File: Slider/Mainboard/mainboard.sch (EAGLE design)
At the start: 11 parts, among them IC1 7805TV, U1 ATMEGA328P_PDIP

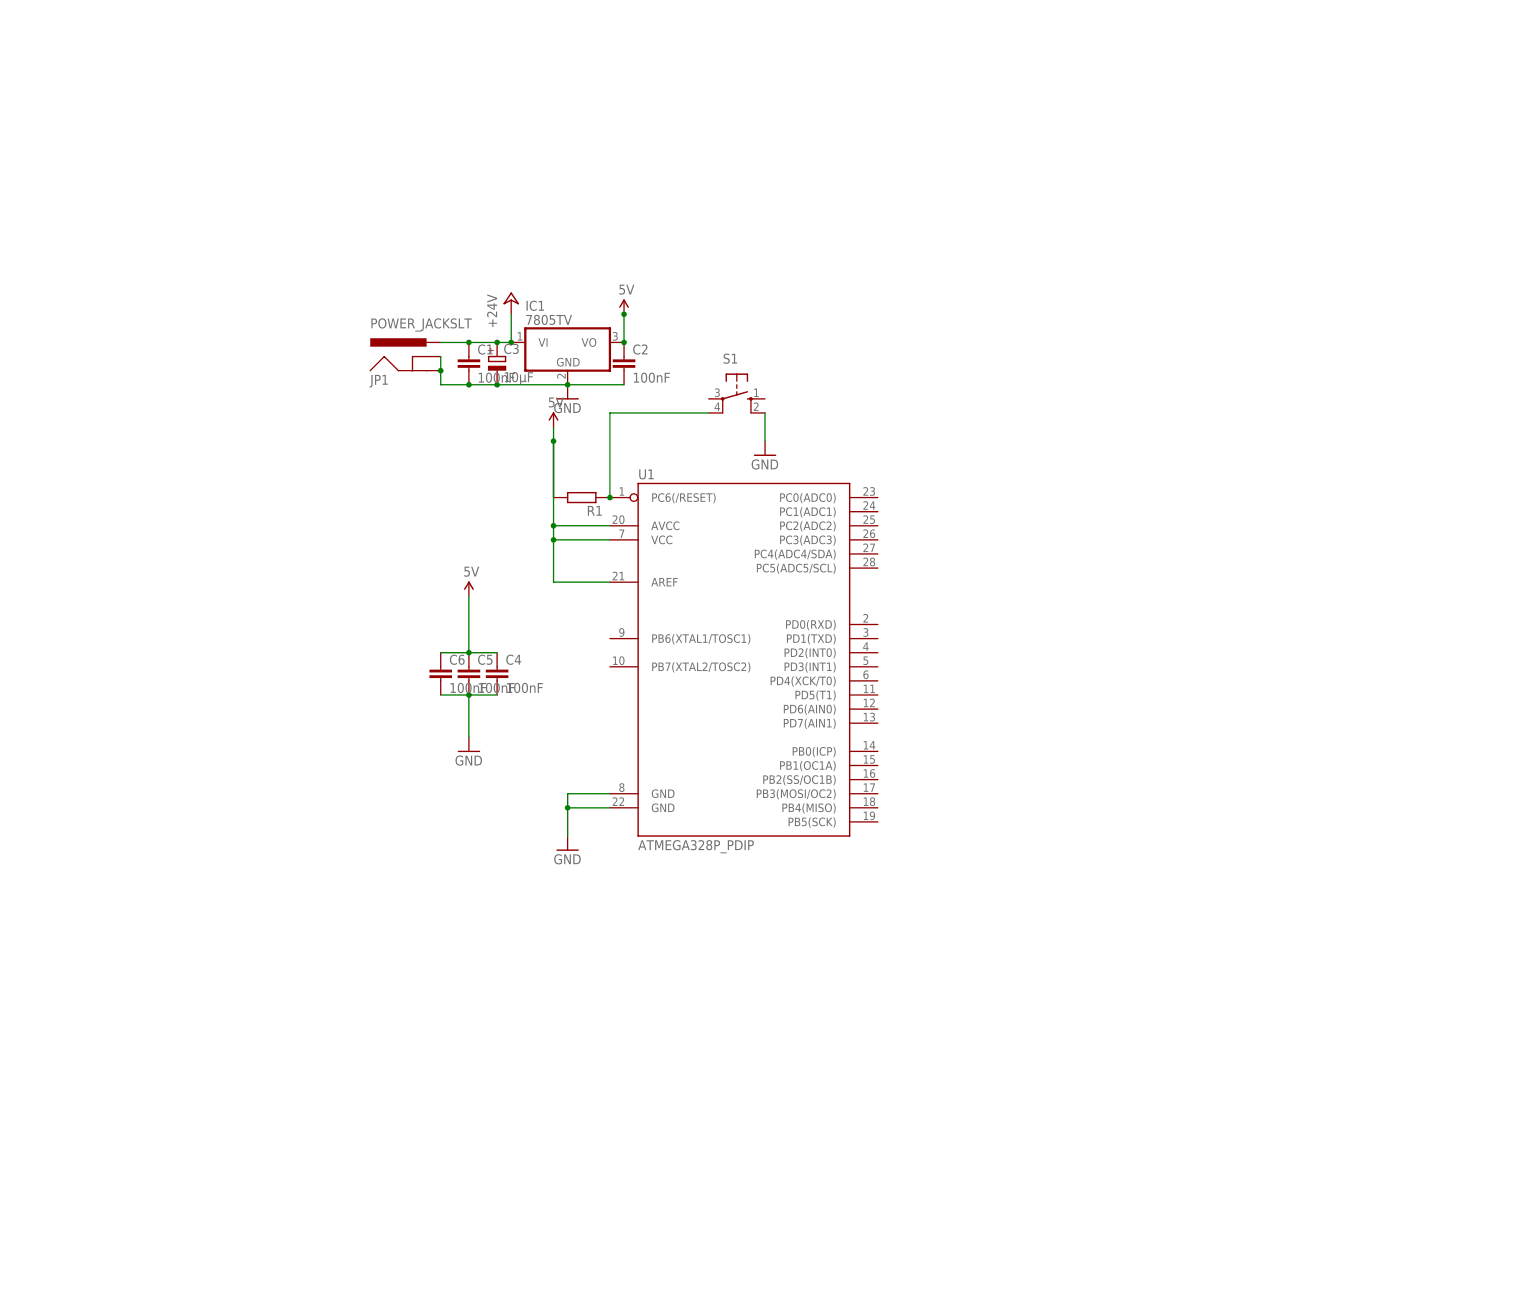
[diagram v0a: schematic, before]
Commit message: Added Motor Drivers, Serial Interface and ICSP Header to schematic
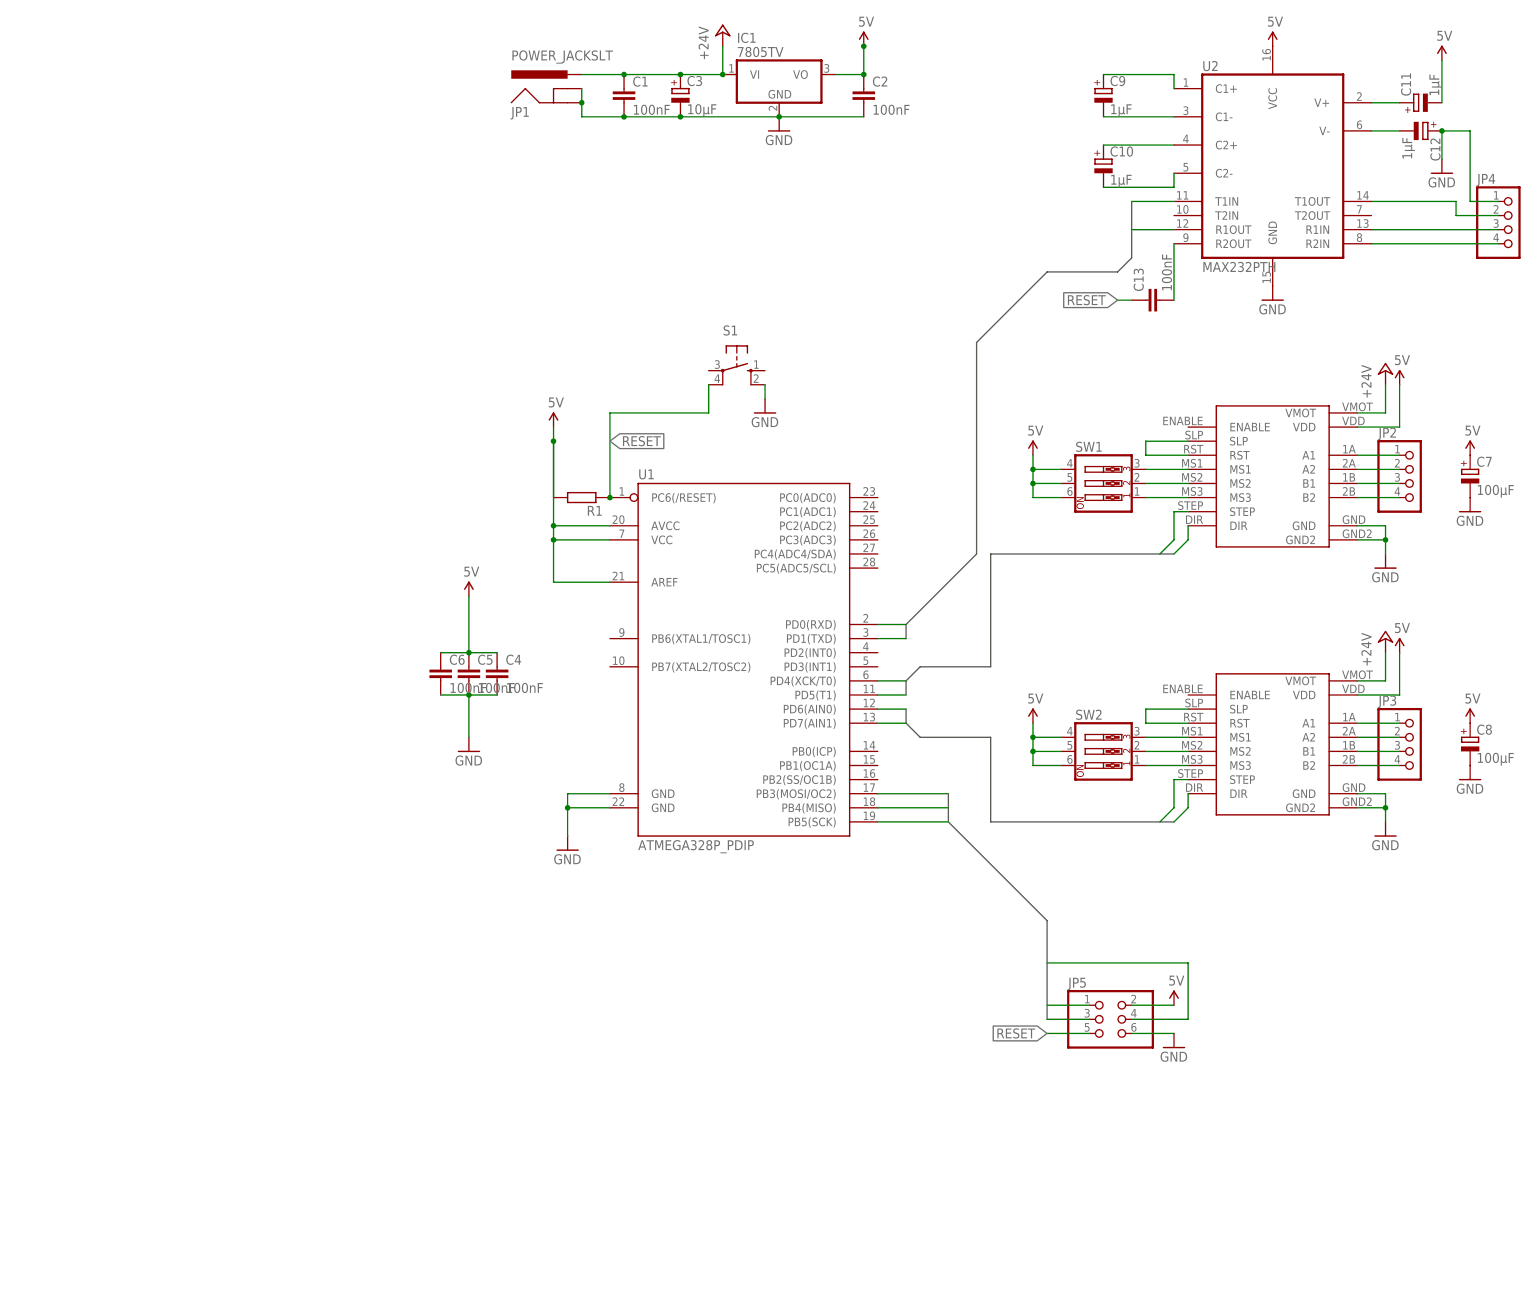
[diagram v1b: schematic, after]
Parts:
- added C10, C11, C12, C9: 1µF, rcl:CPOL-EUE2,5-6E
- added C13: 100nF, rcl:C-EU050-024X044
- added C7, C8: 100µF, rcl:CPOL-EUE2,5-6E
- added JP2, JP3, JP4: (no value), pinhead:PINHD-1X4
- added JP5: (no value), SparkFun-Connectors:PINHD-2X3
- added SW1, SW2: (no value), special:SW_DIP-3
- added U$1, U$2: A4988, parts:A4988
- added U2: MAX232PTH, SparkFun-DigitalIC:MAX232PTH
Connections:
- new net DIR: U$1.DIR, U$2.DIR, U1.PD5(T1), U1.PD7(AIN1)
- new net MISO: JP5.1, U1.PB4(MISO)
- new net MOSI: JP5.4, U1.PB3(MOSI/OC2)
- new net N$1: U$1.RST, U$1.SLP
- new net N$11: SW2.1, U$2.MS3
- new net N$12: SW2.2, U$2.MS2
- new net N$13: SW2.3, U$2.MS1
- new net N$14: JP3.1, U$2.A1
- new net N$15: JP3.2, U$2.A2
- new net N$16: JP3.3, U$2.B1
- new net N$17: JP3.4, U$2.B2
- new net N$18: JP4.2, U2.T1OUT
- new net N$19: JP4.3, U2.R1IN
- new net N$2: JP2.1, U$1.A1
- new net N$20: C9.+, U2.C1+
- new net N$21: C9.-, U2.C1-
- new net N$22: C10.+, U2.C2+
- new net N$23: C10.-, U2.C2-
- new net N$24: C11.+, U2.V+
- new net N$25: C12.-, U2.V-
- new net N$26: JP4.4, U2.R2IN
- new net N$3: JP2.2, U$1.A2
- new net N$4: JP2.3, U$1.B1
- new net N$5: JP2.4, U$1.B2
- new net N$6: SW1.1, U$1.MS3
- new net N$7: SW1.2, U$1.MS2
- new net N$8: SW1.3, U$1.MS1
- new net N$9: U$2.RST, U$2.SLP
- new net RESET: C13.1, JP5.5, R1.1, S1.P1, U1.PC6(/RESET)
- new net RXD: U1.PD0(RXD), U2.R1OUT
- new net SCK: JP5.3, U1.PB5(SCK)
- new net STEP: U$1.STEP, U$2.STEP, U1.PD4(XCK/T0), U1.PD6(AIN0)
- new net TXD: U1.PD1(TXD), U2.T1IN
- net +24V: now also U$1.VMOT, U$2.VMOT
- net 5V: now also C11.-, C7.+, C8.+, JP5.2, U$1.VDD, U$2.VDD, U2.VCC
- net GND: now also C12.+, C7.-, C8.-, JP4.1, JP5.6, U$1.GND, U$1.GND2, U$2.GND, U$2.GND2, U2.GND
- net N$10: now also C13.2, U2.R2OUT; no longer R1.1, S1.P1, U1.PC6(/RESET)
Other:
- moved on the sheet: C1, C2, C3, IC1, JP1, S1

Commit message: Completed schematic
- added endstop amplifier
- added user interface (switches for manual control)
- added IR emitter circuit
- created wifi module
- added 3.3V rail
- moved debug serial port to PD2 and PD3 (software emulated)
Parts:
- added C14, C15: 100nF, rcl:C-EU050-024X044
- added C16: 10µF, rcl:CPOL-EUE2,5-6E
- added D1: (no value), SparkFun-LED:LED5MM
- added IC2: 33CV, linear:7805TV
- added IC3: LM358, SparkFun-AnalogIC:LM358
- added JP6: IR, pinhead:PINHD-1X2
- added JP7: ENDSTOP, pinhead:PINHD-1X3
- added R10, R11, R12, R3, R4: 100Ω, rcl:R-EU_0411/15
- added R13, R14, R2, R5, R6, R7, R8, R9: 10kΩ, rcl:R-EU_0411/15
- added R15: 100kΩ, rcl:R-EU_0411/15
- added S2: LEFT, switch-omron:10-XX
- added S3: TILT CW, switch-omron:10-XX
- added S4: RIGHT, switch-omron:10-XX
- added S5: TILT CCW, switch-omron:10-XX
- added S6: HOMING, switch-omron:10-XX
- added T1, T2: BC337, transistor:BC337
- added U$3: ESP8266, parts:ESP8266
- JP2: value (none) -> MOT1
- JP3: value (none) -> MOT2
- JP4: value (none) -> RS232
- JP5: value (none) -> ICSP
- R1: value (none) -> 10kΩ
- S1: value (none) -> RESET
- SW1: value (none) -> MS MOT1
- SW2: value (none) -> MS MOT2
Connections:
- new net 3.3V: C15.1, IC2.VO, R2.2, U$3.VDD
- new net ESPRX: U$3.RX, U1.PD1(TXD)
- new net ESPTX: U$3.TX, U1.PD0(RXD)
- new net HOMING: R9.1, S6.S, S6.S1, U1.PC4(ADC4/SDA)
- new net LEFT: R5.1, S2.S, S2.S1, U1.PC0(ADC0)
- new net N$27: R2.1, U$3.CH_PD
- new net N$28: R4.2, T1.B
- new net N$29: R3.2, T1.C
- new net N$30: JP6.1, T1.E
- new net N$31: R4.1, U1.PB1(OC1A)
- new net N$32: D1.A, T2.E
- new net N$33: R10.2, T2.B
- new net N$34: R11.2, T2.C
- new net N$35: JP7.1, R12.2
- new net N$36: IC3G1.-IN, JP7.2
- new net N$37: IC3G1.+IN, R13.2, R14.1, R15.2
- new net N$38: IC3G1.OUT, R15.1, U1.PB0(ICP)
- new net RIGHT: R7.1, S4.S, S4.S1, U1.PC1(ADC1)
- new net STATUS: R10.1, U1.PC5(ADC5/SCL)
- new net TILTCCW: R8.1, S5.S, S5.S1, U1.PC3(ADC3)
- new net TILTCW: R6.1, S3.S, S3.S1, U1.PC2(ADC2)
- net 5V: now also C14.1, C16.+, IC2.VI, IC3G1.V+, R11.1, R12.1, R13.1, R3.1, S2.P, S2.P1, S3.P, S3.P1, S4.P, S4.P1, S5.P, S5.P1, S6.P, S6.P1
- net GND: now also C14.2, C15.2, C16.-, D1.C, IC2.GND, IC3G1.V-, JP6.2, JP7.3, R14.2, R5.2, R6.2, R7.2, R8.2, R9.2, U$3.GND
- net RESET: now also S1.P
- net RXD: now also U1.PD2(INT0); no longer U1.PD0(RXD)
- net TXD: now also U1.PD3(INT1); no longer U1.PD1(TXD)
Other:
- moved on the sheet: C1, C2, C3, C4, C5, C6, IC1, JP1, JP5, S1

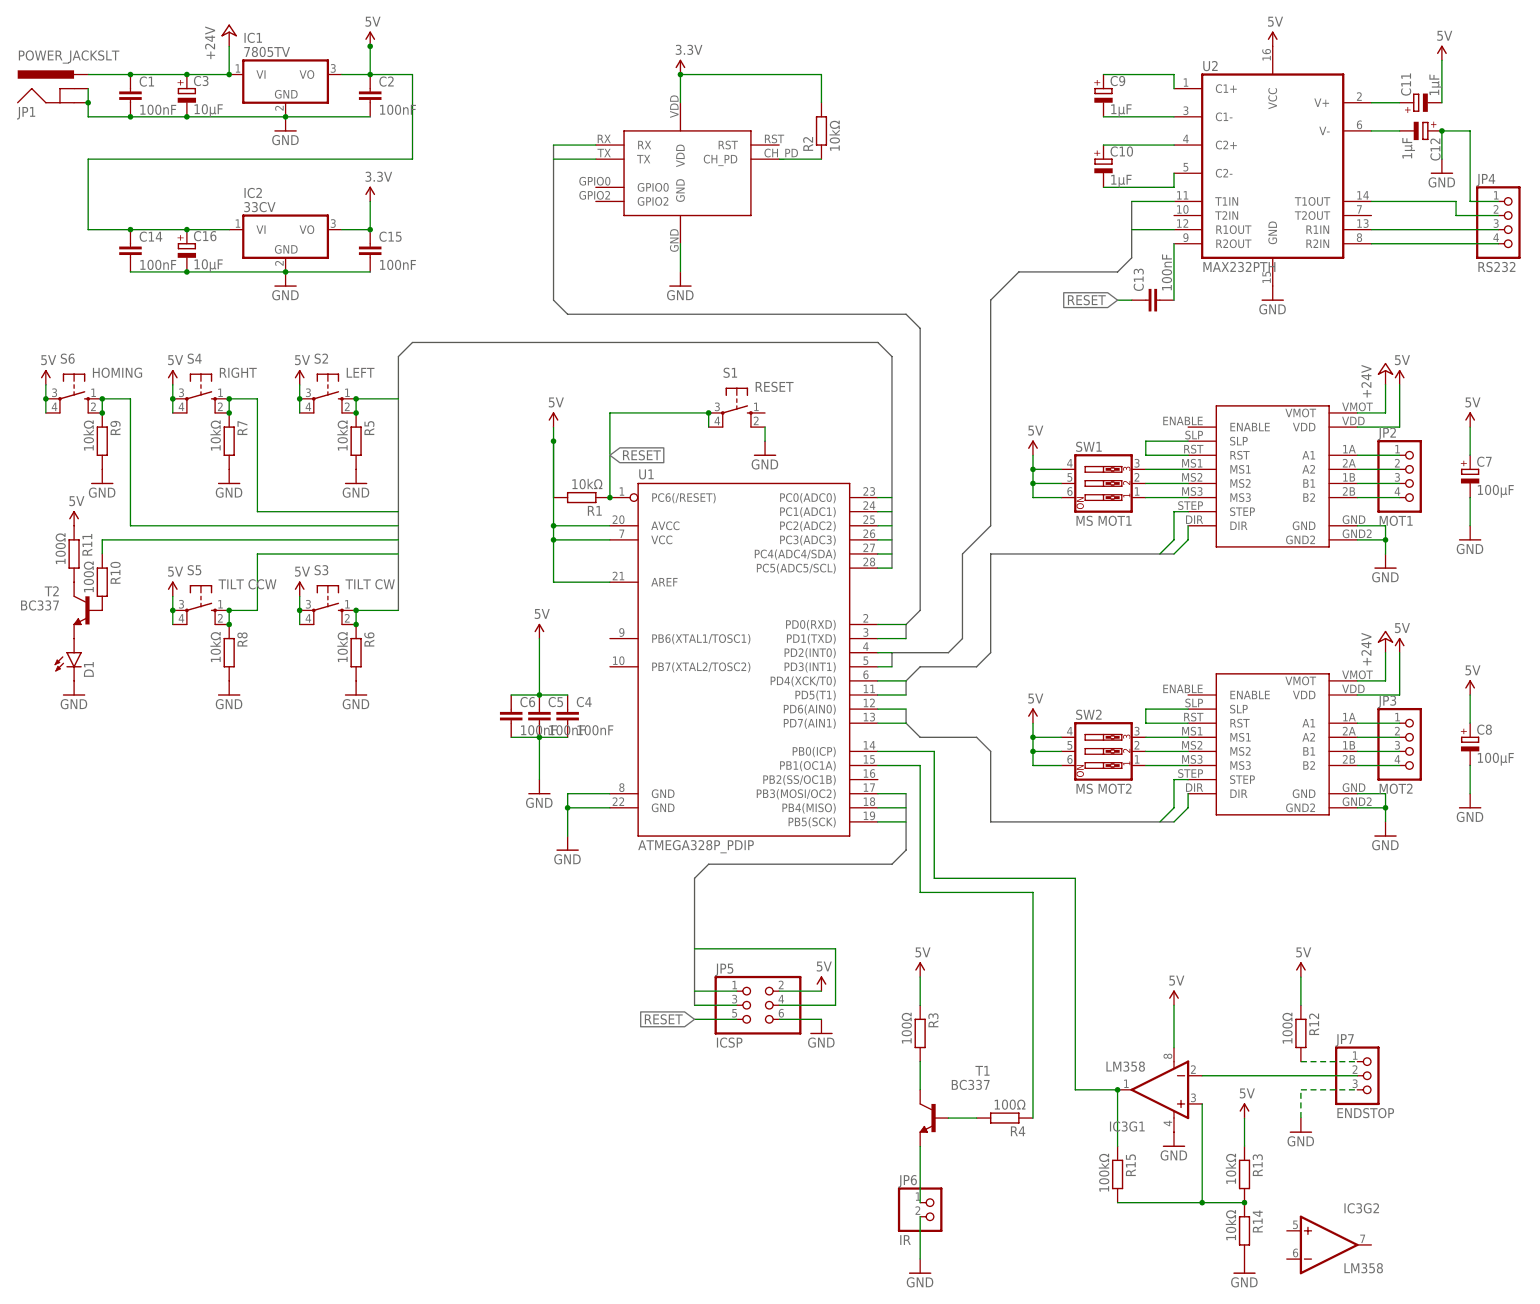
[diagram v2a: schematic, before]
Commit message: small relayout of the schematic
no functional changes
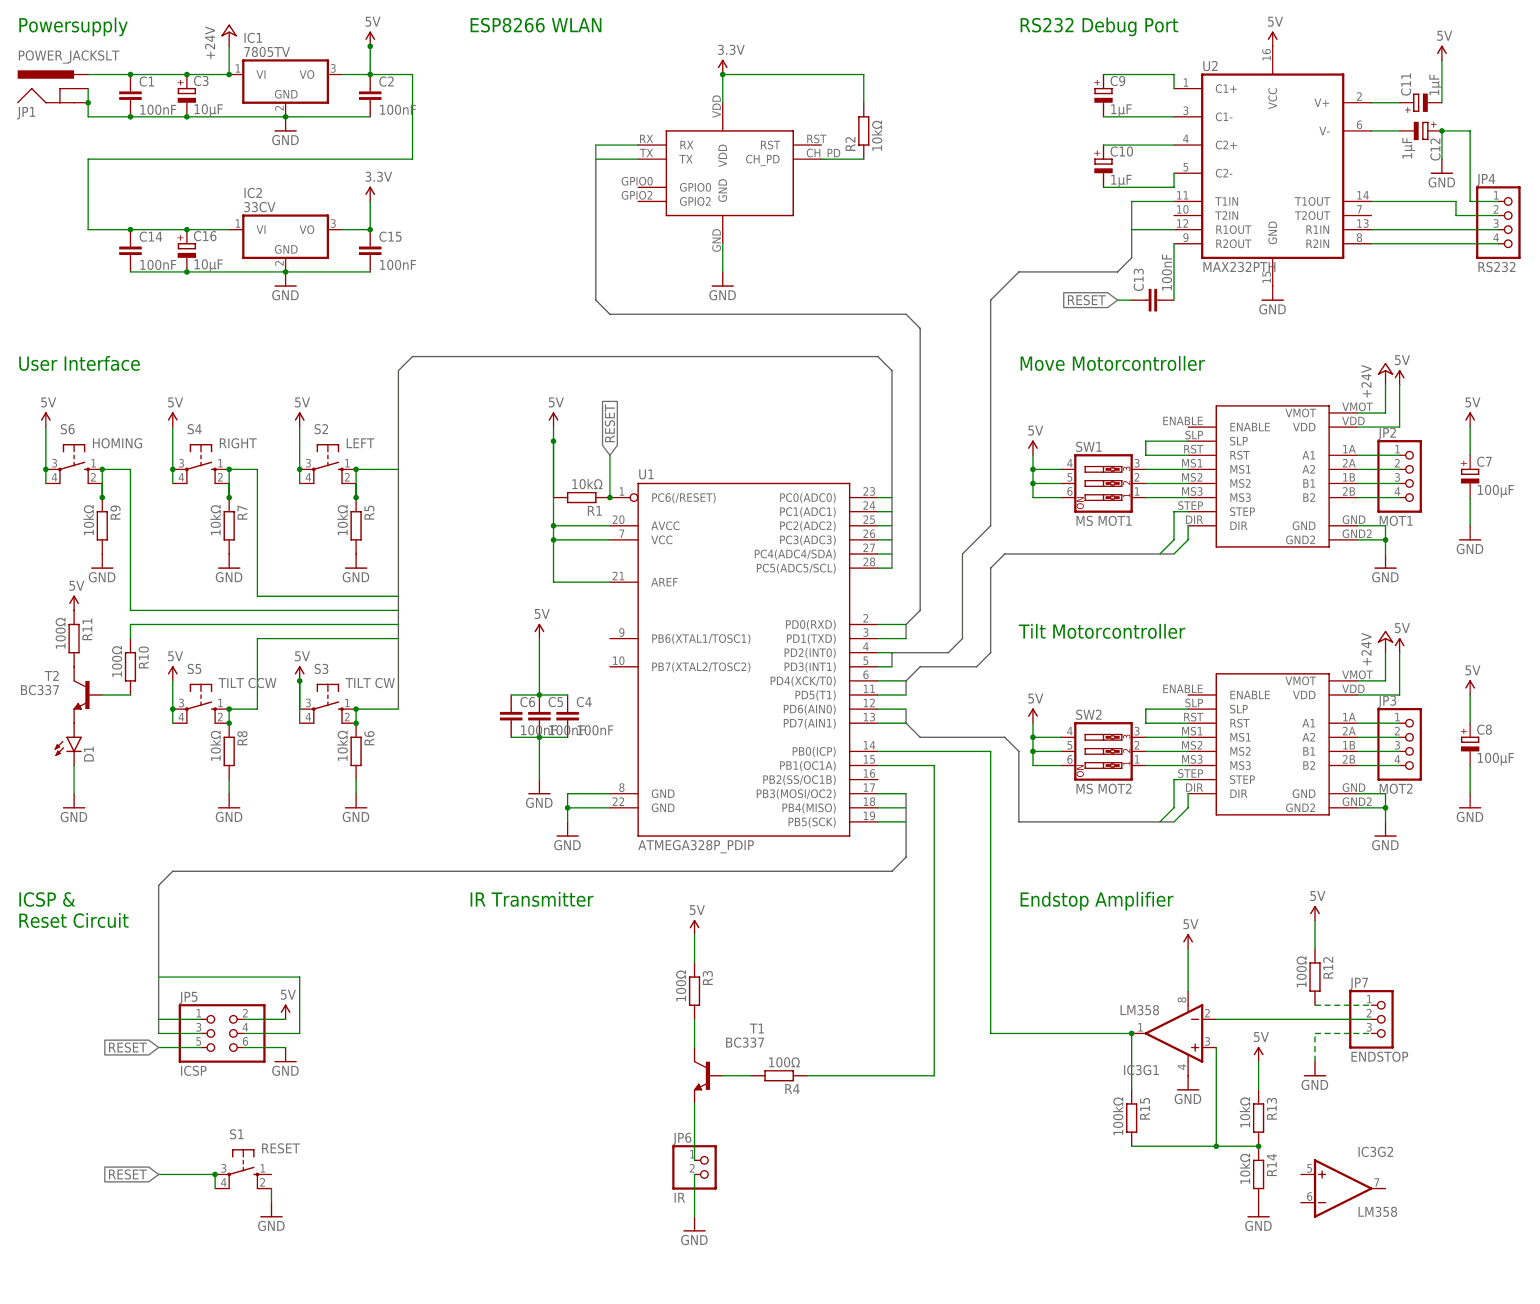
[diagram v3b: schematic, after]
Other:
- note added: "ESP8266 WLAN"
- note added: "Endstop Amplifier"
- note added: "ICSP & Reset Circuit"
- note added: "IR Transmitter"
- note added: "Move Motorcontroller"
- note added: "Powersupply"
- note added: "RS232 Debug Port"
- note added: "Tilt Motorcontroller"
- note added: "User Interface"
- moved on the sheet: D1, IC3G1, IC3G2, JP5, JP6, JP7, R10, R11, R12, R13, R14, R15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
